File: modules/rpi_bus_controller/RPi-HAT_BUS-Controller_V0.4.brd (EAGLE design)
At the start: 65 x 56 mm, 69 parts, among them IC1 MC34063AD, IC2 ADUM1201ARZ, IC3 P89LPC922FDH,512FDH, IC4 24LC-I/OT, IC5 LPC1115, Q1 ASF1, T1 BC856, T2 BCP52, T3 BC847

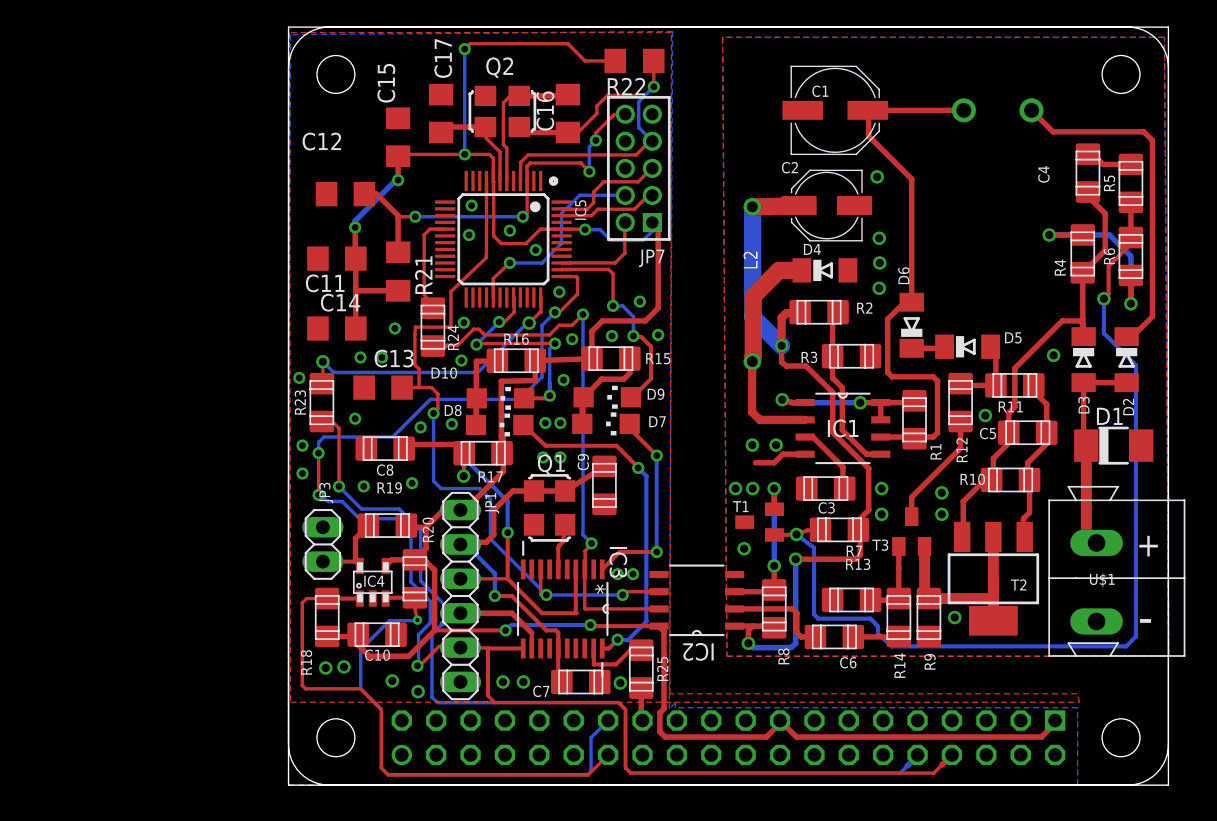
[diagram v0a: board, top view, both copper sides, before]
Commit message: Add TX/RX resistors and decoupling capacitors for ADUM.
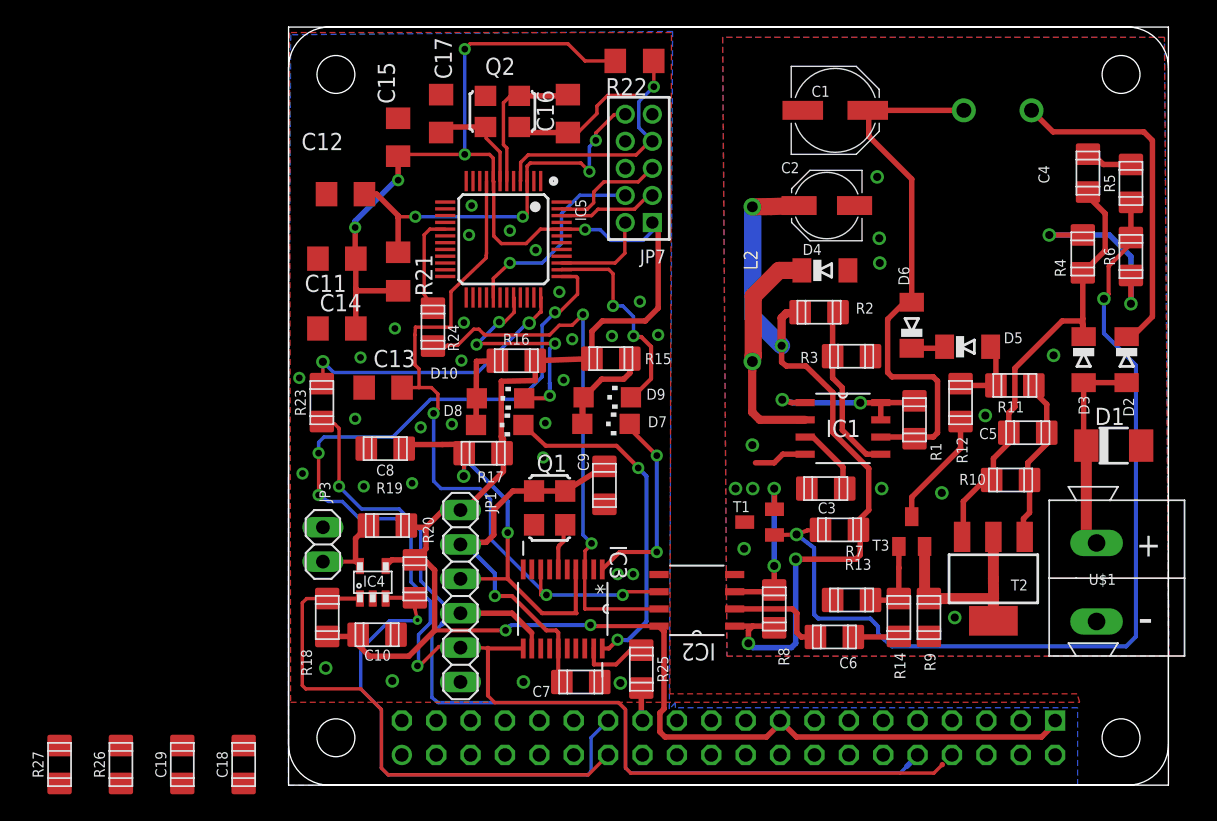
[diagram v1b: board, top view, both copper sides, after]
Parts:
- added C18, C19: 100nF, RCL_for_Selfbus-Projects:R1206
- added R26, R27: 330, RCL_for_Selfbus-Projects:R1206
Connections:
- new net N$15: R26.2
- new net N$16: R27.2
- new net N$17: JP2.8, R26.1
- new net N$18: JP2.10, R27.1
- net +3V3: now also C19.2
- net +3V3/2: now also C18.2
- net GND: now also C19.1
- net GND/2: now also C18.1
- net RXD: no longer JP2.8
- net TXD: no longer JP2.10
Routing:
- net RXD: track 102.9 -> 101.9 mm
- net GND/2: vias 36 -> 29
- net GND: vias 18 -> 14
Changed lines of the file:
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@@
 <attribute name="VALUE" x="24.511" y="9.0297" size="0.8128" layer="27" font="vector" ratio="10" rot="R90" align="center"/>
 </element>
+<element name="C18" library="RCL_for_Selfbus-Projects" package="R1206" value="100nF" x="-3.3147" y="1.524"/>
+<element name="C19" library="RCL_for_Selfbus-Projects" package="R1206" value="100nF" x="-7.8486" y="1.524"/>
+<element name="R26" library="RCL_for_Selfbus-Projects" package="R1206" value="330" x="-12.3825" y="1.524"/>
+<element name="R27" library="RCL_for_Selfbus-Projects" package="R1206" value="330" x="-16.9164" y="1.524"/>
 </elements>
 <signals>
@@
 <wire x1="34.29" y1="34.5948" x2="34.29" y2="42.6974" width="1.27" layer="16"/>
 <wire x1="34.29" y1="42.6974" x2="34.2646" y2="42.7228" width="1.27" layer="16"/>
+<contactref element="C19" pad="2"/>
+<wire x1="-7.8486" y1="0.124" x2="32.9565" y2="11.7475" width="0" layer="19" extent="1-1"/>
 </signal>
 <signal name="SDA">
@@
 <wire x1="9.763125" y1="18.811875" x2="9.763125" y2="15.08125" width="0.254" layer="16"/>
 <wire x1="9.763125" y1="15.08125" x2="12.144375" y2="12.7" width="0.254" layer="16"/>
-<contactref element="JP2" pad="10"/>
-<wire x1="46.47" y1="2.23" x2="46.47" y2="2.17875" width="0.4064" layer="16"/>
 <wire x1="46.47" y1="2.17875" x2="45.67625" y2="1.385" width="0.4064" layer="16"/>
 <contactref element="R23" pad="2"/>
@@
 <wire x1="3.96875" y1="20.955" x2="2.936875" y2="20.955" width="0.254" layer="16"/>
 <wire x1="2.936875" y1="20.955" x2="2.2225" y2="21.43125" width="0.254" layer="16"/>
-<contactref element="JP2" pad="8"/>
 <wire x1="48.295625" y1="1.512" x2="48.295625" y2="1.515625" width="0.4064" layer="1"/>
-<wire x1="48.295625" y1="1.515625" x2="49.01" y2="2.23" width="0.4064" layer="1"/>
 <wire x1="2.619375" y1="25.7175" x2="2.2225" y2="25.320625" width="0.254" layer="16"/>
 <wire x1="2.2225" y1="25.320625" x2="2.2225" y2="24.526875" width="0.254" layer="16"/>
@@
 <via x="34.29" y="21.9075" extent="1-16" drill="0.6" shape="square"/>
 <via x="33.655" y="17.4625" extent="1-16" drill="0.6" shape="square"/>
-<via x="48.26" y="20.0025" extent="1-16" drill="0.6" shape="square"/>
-<via x="43.815" y="20.0025" extent="1-16" drill="0.6" shape="square"/>
 <via x="43.815" y="21.9075" extent="1-16" drill="0.6" shape="square"/>
 <via x="49.2125" y="12.3825" extent="1-16" drill="0.6" shape="square"/>
 <via x="43.6372" y="40.3987" extent="1-16" drill="0.6" shape="square"/>
 <via x="43.6753" y="38.5699" extent="1-16" drill="0.6" shape="square"/>
-<via x="43.6372" y="36.703" extent="1-16" drill="0.6" shape="square"/>
-<via x="36.0172" y="25.1206" extent="1-16" drill="0.6" shape="square"/>
 <via x="34.2646" y="25.1206" extent="1-16" drill="0.6" shape="square"/>
 <via x="43.4848" y="44.9326" extent="1-16" drill="0.6" shape="square"/>
+<contactref element="C19" pad="1"/>
+<wire x1="32.9565" y1="15.5575" x2="-7.8486" y2="2.924" width="0" layer="19" extent="1-1"/>
 </signal>
 <signal name="+3V3/2">
@@
 <wire x1="27.7368" y1="11.3538" x2="27.3685" y2="11.7221" width="0.4064" layer="1"/>
 <wire x1="27.3685" y1="11.7221" x2="27.3685" y2="11.7475" width="0.4064" layer="1"/>
+<contactref element="C18" pad="2"/>
+<wire x1="-3.3147" y1="0.124" x2="2.8575" y2="10.9825" width="0" layer="19" extent="1-1"/>
 </signal>
 <signal name="GND/2">
@@
 </polygon>
 <via x="17.351375" y="7.62" extent="1-16" drill="0.6"/>
-<via x="15.84325" y="7.62" extent="1-16" drill="0.6"/>
-<via x="9.572625" y="6.905625" extent="1-16" drill="0.6"/>
+<wire x1="15.84325" y1="7.62" x2="15.84325" y2="7.62" width="0" layer="19" extent="1-16"/>
+<wire x1="9.572625" y1="6.905625" x2="9.572625" y2="6.905625" width="0" layer="19" extent="1-16"/>
 <via x="7.667625" y="7.699375" extent="1-16" drill="0.6"/>
 <contactref element="C16" pad="1"/>
@@
 <via x="20.955" y="32.940625" extent="1-16" drill="0.5"/>
 <via x="20.32" y="29.924375" extent="1-16" drill="0.5"/>
-<via x="20.081875" y="26.749375" extent="1-16" drill="0.5"/>
-<via x="20.081875" y="24.209375" extent="1-16" drill="0.5"/>
+<wire x1="20.081875" y1="26.749375" x2="20.081875" y2="26.749375" width="0" layer="19" extent="1-16"/>
+<wire x1="20.081875" y1="24.209375" x2="20.081875" y2="24.209375" width="0" layer="19" extent="1-16"/>
 <via x="9.128125" y="22.304375" extent="1-16" drill="0.5"/>
 <via x="5.55625" y="22.06625" extent="1-16" drill="0.5"/>
 <via x="1.031875" y="23.01875" extent="1-16" drill="0.5"/>
-<via x="1.031875" y="25.0825" extent="1-16" drill="0.5"/>
+<wire x1="1.031875" y1="25.0825" x2="1.031875" y2="25.0825" width="0" layer="19" extent="1-16"/>
 <via x="9.763125" y="26.431875" extent="1-16" drill="0.5"/>
 <via x="12.065" y="26.67" extent="1-16" drill="0.5"/>
-<via x="6.905625" y="31.59125" extent="1-16" drill="0.5"/>
+<wire x1="6.905625" y1="31.59125" x2="6.905625" y2="31.59125" width="0" layer="19" extent="1-16"/>
 <via x="5.318125" y="31.59125" extent="1-16" drill="0.5"/>
 <via x="18.970625" y="26.749375" extent="1-16" drill="0.5"/>
 <via x="18.811875" y="24.209375" extent="1-16" drill="0.5"/>
 <via x="23.891875" y="33.17875" extent="1-16" drill="0.5"/>
-<via x="4.09575" y="8.73125" extent="1-16" drill="0.6"/>
+<wire x1="4.09575" y1="8.73125" x2="4.09575" y2="8.73125" width="0" layer="19" extent="1-16"/>
 <via x="2.746375" y="8.651875" extent="1-16" drill="0.6"/>
 <via x="0.79375" y="30.083125" extent="1-16" drill="0.5"/>
@@
 <wire x1="26.0604" y1="4.8596" x2="26.0604" y2="7.1725" width="0.4064" layer="1"/>
 <via x="24.514175" y="7.5438" extent="1-16" drill="0.6"/>
+<contactref element="C18" pad="1"/>
+<wire x1="2.746375" y1="8.651875" x2="-3.3147" y2="2.924" width="0" layer="19" extent="1-1"/>
 </signal>
 <signal name="EIB_IN">
@@
 <wire x1="25.4792" y1="9.9725" x2="26.0604" y2="9.9725" width="0.4064" layer="1"/>
 </signal>
+<signal name="N$15">
+<contactref element="R26" pad="2"/>
+</signal>
+<signal name="N$16">
+<contactref element="R27" pad="2"/>
+</signal>
+<signal name="N$17">
+<contactref element="JP2" pad="8"/>
+<contactref element="R26" pad="1"/>
+<wire x1="-12.3825" y1="2.924" x2="49.01" y2="2.23" width="0" layer="19" extent="1-1"/>
+</signal>
+<signal name="N$18">
+<contactref element="JP2" pad="10"/>
+<contactref element="R27" pad="1"/>
+<wire x1="-16.9164" y1="2.924" x2="46.47" y2="2.23" width="0" layer="19" extent="1-1"/>
+</signal>
 </signals>
